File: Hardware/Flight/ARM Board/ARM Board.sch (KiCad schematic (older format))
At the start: 23 parts, among them J1 USB_B_Micro, J2 Conn_01x20_Female, J3 SD_WM6698CT-ND, J4 Conn_01x20_Female, U1 STM32L4x6RxT6, U2 MSP430FR2355, Y1 Crystal_GND23

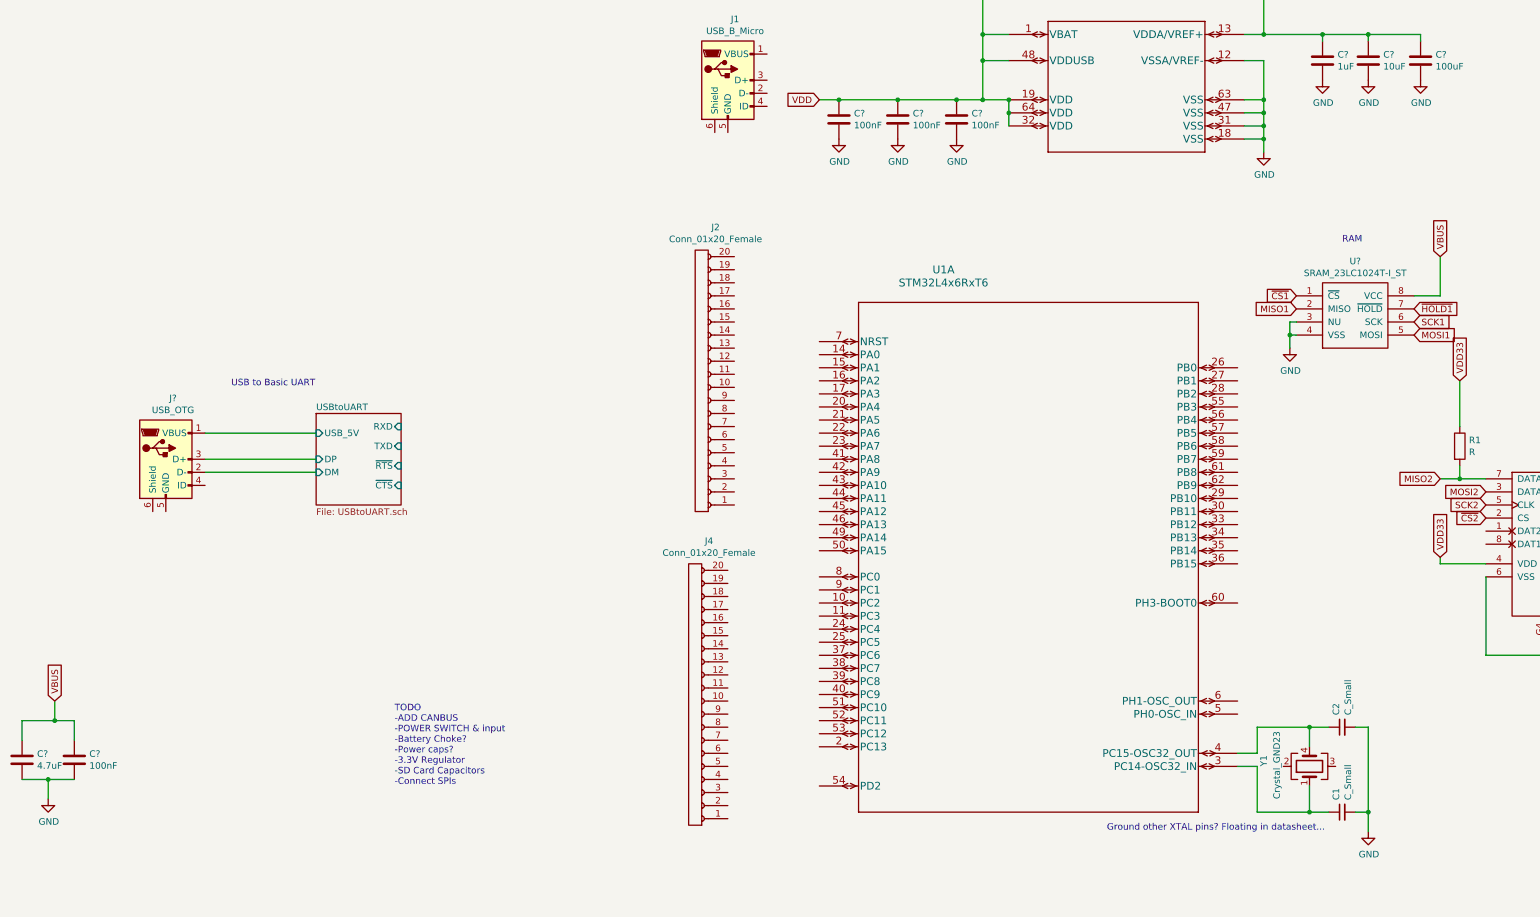
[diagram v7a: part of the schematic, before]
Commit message: Added SPI connections to STM
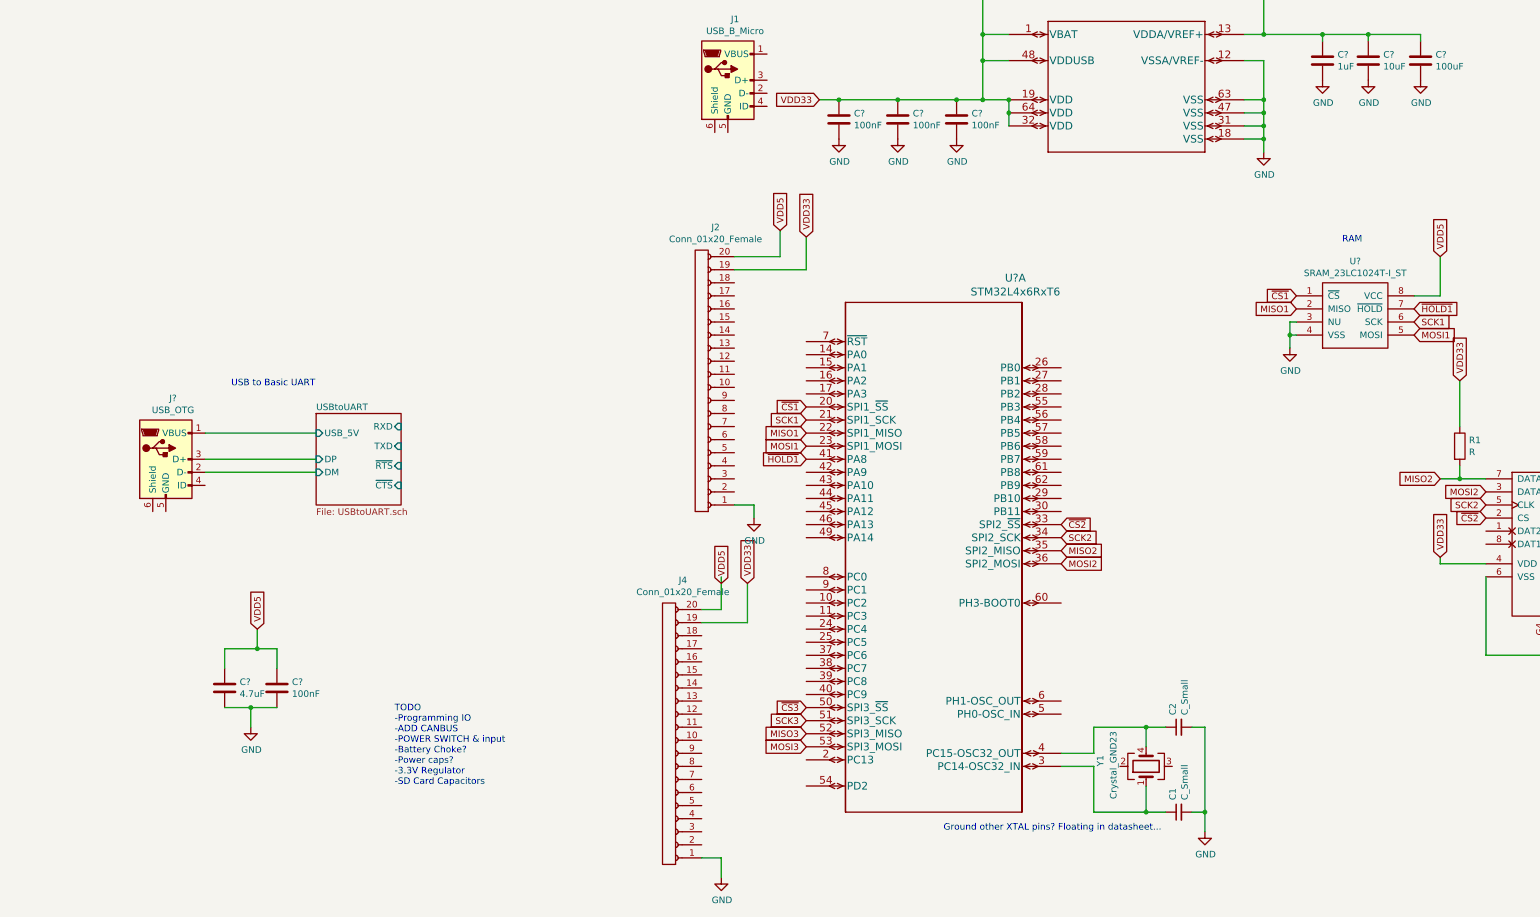
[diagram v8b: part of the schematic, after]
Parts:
- removed unit 1 of U1
- added U?: STM32L4x6RxT6, LQFP64-10x10mm, symbol symbols:STM32L4x6RxT6
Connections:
- net VBUS is gone; now on net VDD5: C?.1, C?.1, U?.8 (VCC)
- net VDD is gone; now on net VDD33: C?.1, C?.1, C?.1, L?.2, U1.1 (VBAT), U1.19 (VDD), U1.32 (VDD), U1.48 (VDDUSB), U1.64 (VDD)
- net GND: now also J2.1 (Pin_1), J4.1 (Pin_1)
- net MISO1: now also U?.22 (SPI1_MISO)
- net MISO2: now also U?.35 (SPI2_MISO)
- net MISO3: now also U?.52 (SPI3_MISO)
- net MOSI1: now also U?.23 (SPI1_MOSI)
- net MOSI2: now also U?.36 (SPI2_MOSI)
- net MOSI3: now also U?.53 (SPI3_MOSI)
- net SCK1: now also U?.21 (SPI1_SCK)
- net SCK2: now also U?.34 (SPI2_SCK)
- net SCK3: now also U?.51 (SPI3_SCK)
- net VDD33: now also J2.19 (Pin_19), J4.19 (Pin_19)
- net ~CS1: now also U?.20 (SPI1_~SS)
- net ~CS2: now also U?.33 (SPI2_~SS)
- net ~CS3: now also U?.50 (SPI3_~SS)
- net ~HOLD1: now also U?.41 (PA8)
- net at C1.1, Y1.1: now also U?.3 (PC14-OSC32_IN)
- net at C2.1, Y1.4: now also U?.4 (PC15-OSC32_OUT)
- net VDD5: now reaches J4.20 (Pin_20)
- net VDD5: now also J2.20 (Pin_20)
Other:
- note added: "TODO\n-Programming IO\n-ADD CANBUS\n-POWER SWITCH & input\n-Battery Choke?\n-Power caps?\n-3.3V Regulator\n-SD Card Capacitors\n"
- note removed: "TODO\n-ADD CANBUS\n-POWER SWITCH & input\n-Battery Choke?\n-Power caps?\n-3.3V Regulator\n-SD Card Capacitors\n-Connect SPIs"
- moved on the sheet: C1, C2, C?, J4, Y1
